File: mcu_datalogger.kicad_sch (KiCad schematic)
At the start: 0 parts

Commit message: added symbols to schematic sheet
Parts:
- added BT1: Battery, symbol Device:Battery
- added C1, C2, C3, C4: C, symbol Device:C
- added C5: C_Polarized, symbol Device:C_Polarized
- added D1, D2: LED, symbol Device:LED
- added H1, H2, H3, H4: MountingHole, symbol Mechanical:MountingHole
- added R1, R2, R3, R4, R5, R6, R7: R, symbol Device:R
- added U1, U2: 24LC1025, symbol Memory_EEPROM:24LC1025
- added U3: DS1337S_, DS1337S_:SOIC127P600X175-8N, symbol DS1337S_:DS1337S_
- added U4: ATMEGA328P-AU, ATMEGA328P-AU:QFP80P900X900X120-32N, symbol ATMEGA328P-AU:ATMEGA328P-AU
- added Y1, Y2: Crystal, symbol Device:Crystal
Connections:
- new net: U4.21 (GND), U4.3 (GND), U4.5 (GND)
- new net: U4.4 (VCC), U4.6 (VCC)
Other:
- added sheet connectors (connectors.kicad_sch)

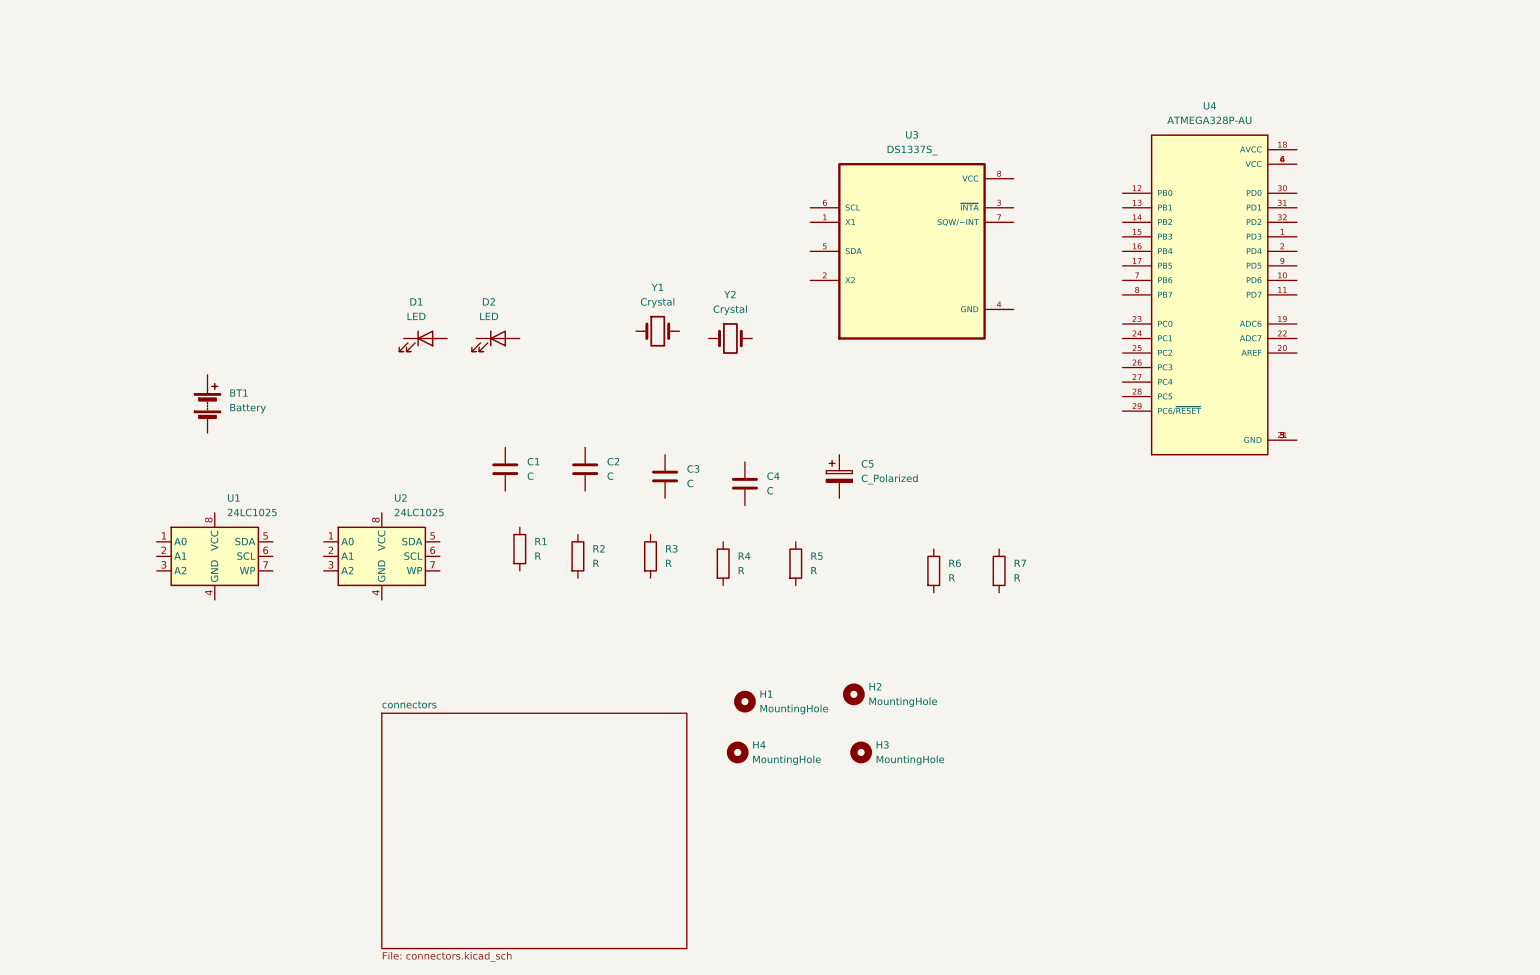
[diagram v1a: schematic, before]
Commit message: added component values
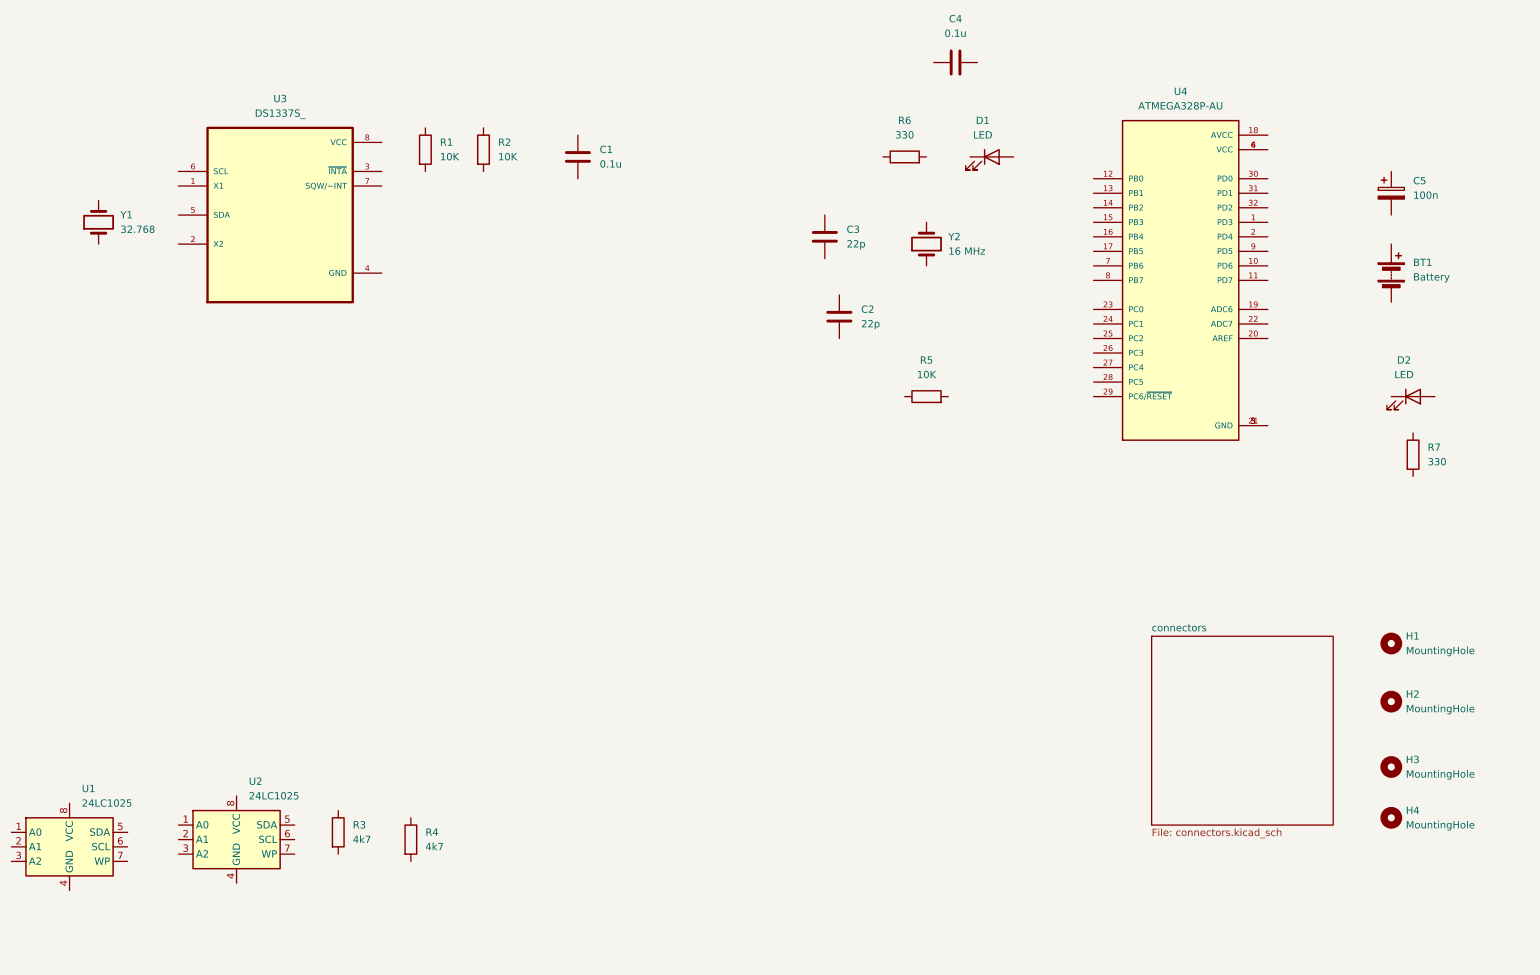
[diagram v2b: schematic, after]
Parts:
- C1, C4: value C -> 0.1u
- C2, C3: value C -> 22p
- C5: value C_Polarized -> 100n
- R1, R2, R5: value R -> 10K
- R3, R4: value R -> 4k7
- R6, R7: value R -> 330
- Y1: value Crystal -> 32.768
- Y2: value Crystal -> 16 MHz
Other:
- moved on the sheet: BT1, C1, C2, C3, C4, C5, D1, D2, H1, H2, H3, H4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

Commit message: associated symbol & footprint
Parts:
- BT1: footprint (none) -> Connector_PinHeader_2.54mm:PinHeader_1x02_P2.54mm_Horizontal
- C1, C2, C3, C4, C5: footprint (none) -> Capacitor_SMD:C_0805_2012Metric
- D1, D2: footprint (none) -> LED_SMD:LED_0805_2012Metric
- H1, H2, H3, H4: footprint (none) -> MountingHole:MountingHole_2.2mm_M2
- R1, R2, R3, R4, R5, R6, R7: footprint (none) -> Resistor_SMD:R_0805_2012Metric
- U1, U2: footprint (none) -> Package_SO:SOIC-8_5.3x5.3mm_P1.27mm
- U3: footprint DS1337S_:SOIC127P600X175-8N -> (none)
- U4: footprint ATMEGA328P-AU:QFP80P900X900X120-32N -> (none)
- Y1, Y2: footprint (none) -> Crystal:Crystal_SMD_5032-2Pin_5.0x3.2mm_HandSoldering
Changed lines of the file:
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@@
 			)
 		)
-		(property "Footprint" ""
+		(property "Footprint" "Crystal:Crystal_SMD_5032-2Pin_5.0x3.2mm_HandSoldering"
 			(at 36.83 52.07 0)
 			(effects
@@
 			)
 		)
-		(property "Footprint" ""
+		(property "Footprint" "Capacitor_SMD:C_0805_2012Metric"
 			(at 263.8552 50.8 0)
 			(effects
@@
 			)
 		)
-		(property "Footprint" ""
+		(property "Footprint" "Resistor_SMD:R_0805_2012Metric"
 			(at 89.662 160.02 90)
 			(effects
@@
 			)
 		)
-		(property "Footprint" "DS1337S_:SOIC127P600X175-8N"
+		(property "Footprint" ""
 			(at 68.58 50.8 0)
 			(effects
@@
 			)
 		)
-		(property "Footprint" ""
+		(property "Footprint" "LED_SMD:LED_0805_2012Metric"
 			(at 266.7 82.55 0)
 			(effects
@@
 			)
 		)
-		(property "Footprint" ""
+		(property "Footprint" "Crystal:Crystal_SMD_5032-2Pin_5.0x3.2mm_HandSoldering"
 			(at 181.61 55.88 0)
 			(effects
@@
 			)
 		)
-		(property "Footprint" ""
+		(property "Footprint" "Capacitor_SMD:C_0805_2012Metric"
 			(at 164.7952 58.42 0)
 			(effects
@@
 			)
 		)
-		(property "Footprint" ""
+		(property "Footprint" "Capacitor_SMD:C_0805_2012Metric"
 			(at 190.5 23.1648 0)
 			(effects
@@
 			)
 		)
-		(property "Footprint" "ATMEGA328P-AU:QFP80P900X900X120-32N"
+		(property "Footprint" ""
 			(at 226.06 62.23 0)
 			(effects
@@
 			)
 		)
-		(property "Footprint" ""
+		(property "Footprint" "MountingHole:MountingHole_2.2mm_M2"
 			(at 262.89 135.89 0)
 			(effects
@@
 			)
 		)
-		(property "Footprint" ""
+		(property "Footprint" "Resistor_SMD:R_0805_2012Metric"
 			(at 177.8 42.418 90)
 			(effects
@@
 			)
 		)
-		(property "Footprint" ""
+		(property "Footprint" "Connector_PinHeader_2.54mm:PinHeader_1x02_P2.54mm_Horizontal"
 			(at 262.89 59.436 90)
 			(effects
@@
 			)
 		)
-		(property "Footprint" ""
+		(property "Footprint" "MountingHole:MountingHole_2.2mm_M2"
 			(at 262.89 125.73 0)
 			(effects
@@
 			)
 		)
-		(property "Footprint" ""
+		(property "Footprint" "Package_SO:SOIC-8_5.3x5.3mm_P1.27mm"
 			(at 60.96 160.02 0)
 			(effects
@@
 			)
 		)
-		(property "Footprint" ""
+		(property "Footprint" "Resistor_SMD:R_0805_2012Metric"
 			(at 92.202 39.37 90)
 			(effects
@@
 			)
 		)
-		(property "Footprint" ""
+		(property "Footprint" "Resistor_SMD:R_0805_2012Metric"
 			(at 102.362 39.37 90)
 			(effects
@@
 			)
 		)
-		(property "Footprint" ""
+		(property "Footprint" "Resistor_SMD:R_0805_2012Metric"
 			(at 264.922 92.71 90)
 			(effects
@@
 			)
 		)
-		(property "Footprint" ""
+		(property "Footprint" "MountingHole:MountingHole_2.2mm_M2"
 			(at 262.89 156.21 0)
 			(effects
@@
 			)
 		)
-		(property "Footprint" ""
+		(property "Footprint" "Resistor_SMD:R_0805_2012Metric"
 			(at 181.61 84.328 90)
 			(effects
@@
 			)
 		)
-		(property "Footprint" ""
+		(property "Footprint" "LED_SMD:LED_0805_2012Metric"
 			(at 193.04 40.64 0)
 			(effects
@@
 			)
 		)
-		(property "Footprint" ""
+		(property "Footprint" "MountingHole:MountingHole_2.2mm_M2"
 			(at 262.89 147.32 0)
 			(effects
@@
 			)
 		)
-		(property "Footprint" ""
+		(property "Footprint" "Resistor_SMD:R_0805_2012Metric"
 			(at 76.962 158.75 90)
 			(effects
@@
 			)
 		)
-		(property "Footprint" ""
+		(property "Footprint" "Capacitor_SMD:C_0805_2012Metric"
 			(at 121.6152 44.45 0)
 			(effects
@@
 			)
 		)
-		(property "Footprint" ""
+		(property "Footprint" "Capacitor_SMD:C_0805_2012Metric"
 			(at 167.3352 72.39 0)
 			(effects
@@
 			)
 		)
-		(property "Footprint" ""
+		(property "Footprint" "Package_SO:SOIC-8_5.3x5.3mm_P1.27mm"
 			(at 31.75 161.29 0)
 			(effects

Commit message: wired up schematic
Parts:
- U3: footprint (none) -> footprints:SOIC127P600X175-8N
- U4: footprint (none) -> footprints:QFP80P900X900X120-32N
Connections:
- net at Y1.1: now also U3.2 (X2)
- net at Y1.2: now also U3.1 (X1)
- net at C5.1: now also BT1.1 (+), D2.2 (A), U4.18 (AVCC), U4.4 (VCC)
- net GND: now reaches C5.2
- net GND: now also BT1.2 (-), C1.2, C2.1, C3.1, C4.2, R6.1, R7.2, U1.4 (GND), U1.7 (WP), U2.2 (A1), U2.4 (GND), U2.7 (WP), U3.4 (GND), U4.21 (GND), U4.3 (GND), U4.5 (GND)
- net Vcc: now reaches R4.1
- net Vcc: now also R3.1, R5.1, U1.1 (A0), U1.2 (A1), U1.3 (A2), U1.8 (VCC), U2.1 (A0), U2.3 (A2), U2.8 (VCC)
- net SCL: now reaches R4.2
- net SCL: now also U1.6 (SCL), U2.6 (SCL)
- net at U3.3 (~{INTA}): now also R1.2
- net SDA: now reaches U3.5 (SDA)
- net SDA: now also R3.2, U1.5 (SDA), U2.5 (SDA), U4.27 (PC4)
- net SCK: now reaches U3.6 (SCL)
- net SCK: now also D1.2 (A), U4.17 (PB5), U4.28 (PC5)
- net at U3.7 (SQW/~INT): now also R2.2
- net at U3.8 (VCC): now also C1.1, R1.1, R2.1
- net at D2.1 (K): now also R7.1
- net at Y2.1: now also C2.2, U4.8 (PB7)
- net at Y2.2: now also C3.2, U4.7 (PB6)
- net at C4.1: now also U4.20 (AREF)
- net D3: now reaches U4.1 (PD3)
- net D6: now reaches U4.10 (PD6)
- net D7: now reaches U4.11 (PD7)
- net DB: now reaches U4.12 (PB0)
- net MOSI: now reaches U4.15 (PB3)
- net MISO: now reaches U4.16 (PB4)
- net D4: now reaches U4.2 (PD4)
- net RESET: now reaches U4.29 (PC6/~{RESET})
- net RESET: now also R5.2
- net RX: now reaches U4.30 (PD0)
- net TX: now reaches U4.31 (PD1)
- net D2: now reaches U4.32 (PD2)
- net at U4.6 (VCC): no longer U4.4 (VCC)
- net D5: now reaches U4.9 (PD5)
- net at R6.2: now also D1.1 (K)
- no-connect marks 0 -> 9
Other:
- moved on the sheet: BT1, C1, C2, C3, C4, C5, D1, D2, R1, R2, R3, R4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

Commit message: completed wiring
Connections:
- net SCL is gone; now on net SCK: R4.2, U1.6 (SCL), U2.6 (SCL)
- net Vcc: now also C1.1, R1.1, R2.1, U3.8 (VCC)
- net DB renamed D8
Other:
- sheet connectors ports: added D2, D3, D4, D5, D6, D7, D8, GND, MISO, MOSI, RESET, Rx, SCK, SDA, Tx, Vcc; removed none

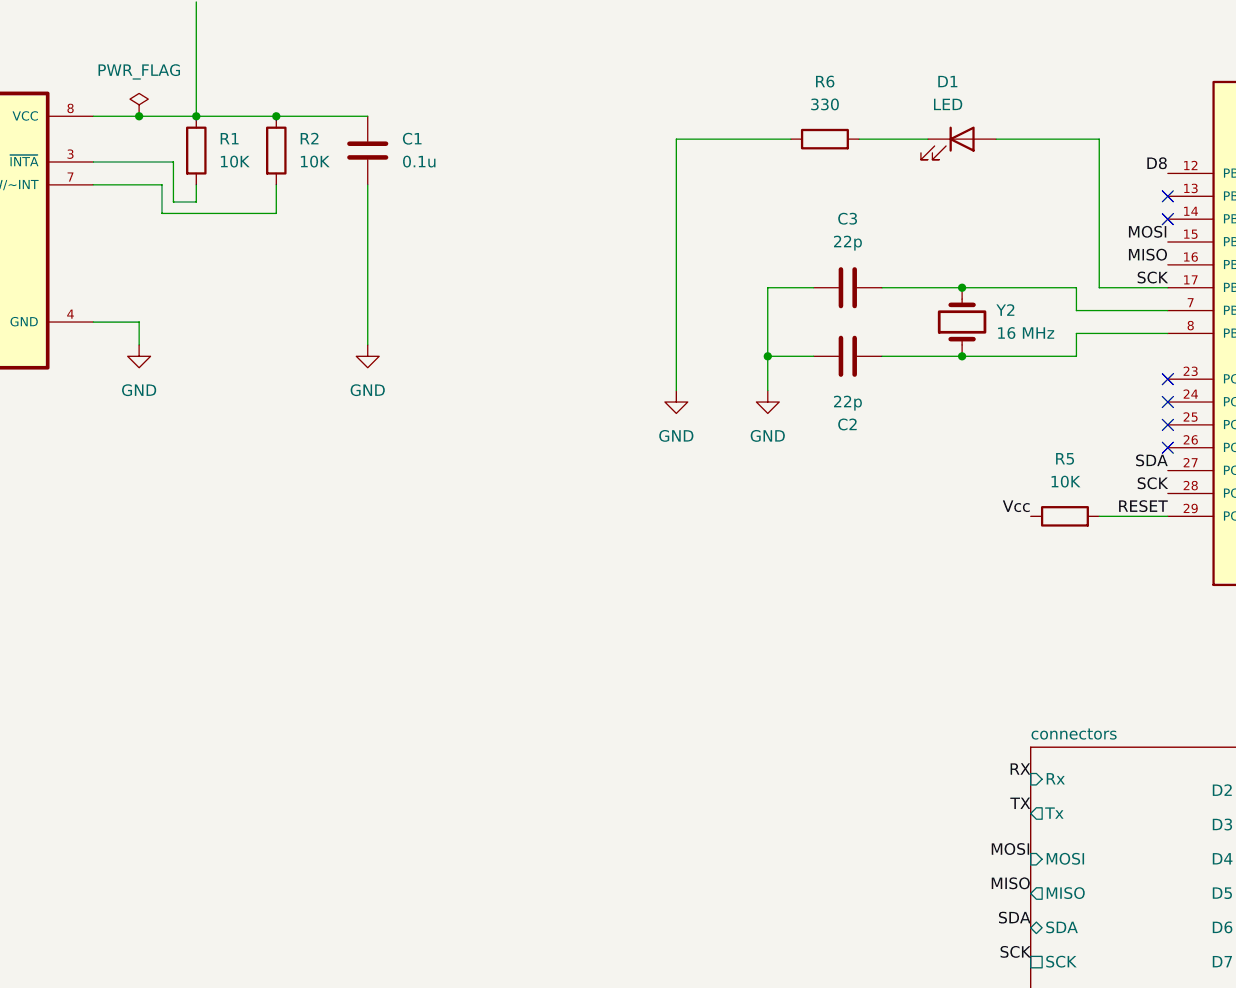
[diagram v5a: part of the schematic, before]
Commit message: fixed ERC with 50mil grid snap
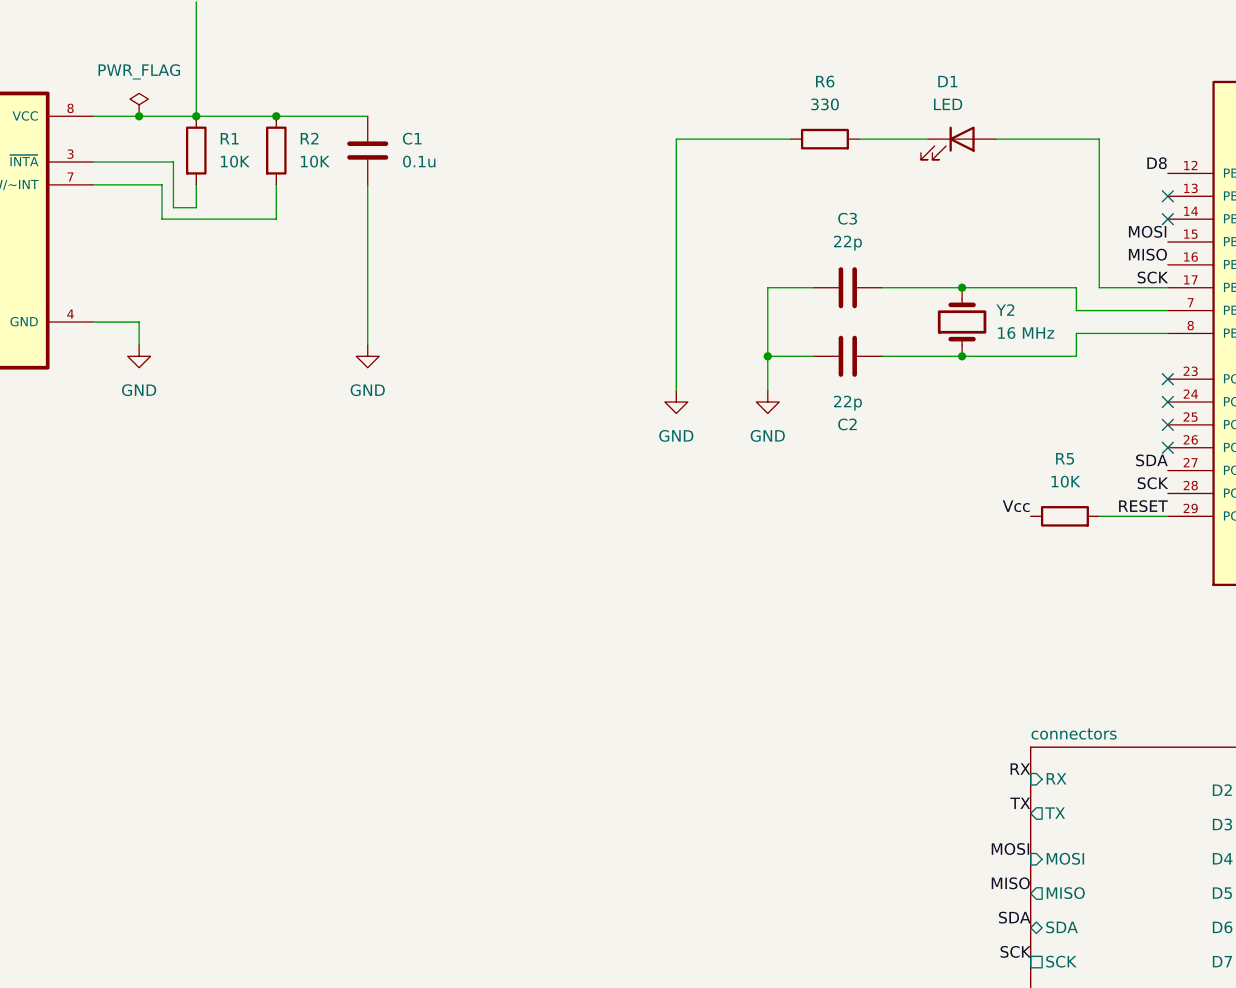
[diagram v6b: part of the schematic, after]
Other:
- sheet connectors ports: added RX, TX; removed Rx, Tx
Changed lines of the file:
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@@
 	(wire
 		(pts
+			(xy 93.98 45.72) (xy 93.98 49.53)
+		)
+		(stroke
+			(width 0)
+			(type default)
+		)
+	)
+	(wire
+		(pts
 			(xy 236.22 87.63) (xy 238.76 87.63)
 		)
@@
 	(wire
 		(pts
-			(xy 93.98 48.895) (xy 106.68 48.895)
+			(xy 93.98 49.53) (xy 106.68 49.53)
 		)
 		(stroke
@@
 	(wire
 		(pts
+			(xy 95.25 43.18) (xy 95.25 48.26)
+		)
+		(stroke
+			(width 0)
+			(type default)
+		)
+	)
+	(wire
+		(pts
 			(xy 161.29 57.15) (xy 161.29 64.77)
 		)
@@
 	(wire
 		(pts
-			(xy 236.22 36.83) (xy 241.3 36.83)
+			(xy 97.79 48.26) (xy 95.25 48.26)
 		)
 		(stroke
@@
 	(wire
 		(pts
-			(xy 35.56 45.72) (xy 35.56 46.99)
+			(xy 236.22 36.83) (xy 241.3 36.83)
 		)
 		(stroke
@@
 	(wire
 		(pts
-			(xy 60.96 172.72) (xy 76.2 172.72)
+			(xy 35.56 45.72) (xy 35.56 46.99)
 		)
 		(stroke
@@
 	(wire
 		(pts
-			(xy 274.32 46.99) (xy 274.32 48.26)
+			(xy 60.96 172.72) (xy 76.2 172.72)
 		)
 		(stroke
@@
 	(wire
 		(pts
-			(xy 163.83 40.64) (xy 151.13 40.64)
+			(xy 274.32 46.99) (xy 274.32 48.26)
 		)
 		(stroke
@@
 	(wire
 		(pts
-			(xy 106.68 48.895) (xy 106.68 45.72)
+			(xy 163.83 40.64) (xy 151.13 40.64)
 		)
 		(stroke
@@
 	(wire
 		(pts
-			(xy 261.62 48.26) (xy 274.32 48.26)
+			(xy 106.68 49.53) (xy 106.68 45.72)
 		)
 		(stroke
@@
 	(wire
 		(pts
-			(xy 186.69 40.64) (xy 198.12 40.64)
+			(xy 261.62 48.26) (xy 274.32 48.26)
 		)
 		(stroke
@@
 	(wire
 		(pts
-			(xy 95.25 43.18) (xy 95.25 47.625)
+			(xy 186.69 40.64) (xy 198.12 40.64)
 		)
 		(stroke
@@
 	(wire
 		(pts
-			(xy 261.62 36.83) (xy 274.32 36.83)
+			(xy 97.79 45.72) (xy 97.79 48.26)
 		)
 		(stroke
@@
 	(wire
 		(pts
-			(xy 93.98 45.72) (xy 93.98 48.895)
+			(xy 261.62 36.83) (xy 274.32 36.83)
 		)
 		(stroke
@@
 	(wire
 		(pts
-			(xy 95.25 47.625) (xy 97.79 47.625)
-		)
-		(stroke
-			(width 0)
-			(type default)
-		)
-	)
-	(wire
-		(pts
 			(xy 86.36 38.1) (xy 91.44 38.1)
 		)
@@
 	(wire
 		(pts
-			(xy 97.79 47.625) (xy 97.79 45.72)
-		)
-		(stroke
-			(width 0)
-			(type default)
-		)
-	)
-	(wire
-		(pts
 			(xy 173.99 57.15) (xy 182.88 57.15)
 		)
@@
 			)
 		)
-		(pin "Rx" input
+		(pin "RX" input
 			(at 190.5 111.76 180)
 			(effects
@@
 			)
 		)
-		(pin "Tx" output
+		(pin "TX" output
 			(at 190.5 115.57 180)
 			(effects

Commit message: added comments to schematic
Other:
- note added: "EEPROM"
- note added: "MCU"
- note added: "Real time clock"
- moved on the sheet: BT1, C2, C3, C4, C5, D1, D2, H1, H2, H3, H4, R3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
